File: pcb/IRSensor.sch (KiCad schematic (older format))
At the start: 39 parts, among them Q2 IRFML8244, Q3 IRFML8244, U2 NJM2746, U3 NJU7098, U4 NJU7098, U5 NJU7098, U6 NJU7098

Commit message: Make netlist
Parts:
- C10, C11, C4, C5, C6, C7, C8, C9: footprint (none) -> Capacitors_SMD:C_0603_HandSoldering
- D2, D3, D4, D5, D6, D7, D8, D9: footprint (none) -> LEDs:LED_D5.0mm_Horizontal_O1.27mm_Z3.0mm
- Q2, Q3: footprint (none) -> TO_SOT_Packages_SMD:SOT-23
- R10, R11, R12, R13, R16, R17, R18, R19, R20, R21, R22, R23, R8, R9: footprint (none) -> Resistors_SMD:R_0603_HandSoldering
- R14, R15: footprint (none) -> Resistors_SMD:R_0805_HandSoldering
- U3, U4, U5, U6: footprint Package_TO_SOT_SMD:TSOT-23-6 -> TO_SOT_Packages_SMD:SOT-23-6_Handsoldering
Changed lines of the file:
@@
 F 0 "R8" H 1320 1796 50  0000 L CNN
 F 1 "10k" V 1250 1700 50  0000 L CNN
-F 2 "" V 1180 1750 50  0001 C CNN
+F 2 "Resistors_SMD:R_0603_HandSoldering" V 1180 1750 50  0001 C CNN
 F 3 "~" H 1250 1750 50  0001 C CNN
 	1    1250 1750
@@
 F 0 "R9" H 1320 2096 50  0000 L CNN
 F 1 "10k" V 1250 2000 50  0000 L CNN
-F 2 "" V 1180 2050 50  0001 C CNN
+F 2 "Resistors_SMD:R_0603_HandSoldering" V 1180 2050 50  0001 C CNN
 F 3 "~" H 1250 2050 50  0001 C CNN
 	1    1250 2050
@@
 F 0 "R10" H 1320 3596 50  0000 L CNN
 F 1 "10k" V 1250 3500 50  0000 L CNN
-F 2 "" V 1180 3550 50  0001 C CNN
+F 2 "Resistors_SMD:R_0603_HandSoldering" V 1180 3550 50  0001 C CNN
 F 3 "~" H 1250 3550 50  0001 C CNN
 	1    1250 3550
@@
 F 0 "R11" H 1320 3896 50  0000 L CNN
 F 1 "10k" V 1250 3800 50  0000 L CNN
-F 2 "" V 1180 3850 50  0001 C CNN
+F 2 "Resistors_SMD:R_0603_HandSoldering" V 1180 3850 50  0001 C CNN
 F 3 "~" H 1250 3850 50  0001 C CNN
 	1    1250 3850
@@
 F 0 "R12" V 2550 1950 50  0000 L CNN
 F 1 "10" V 2650 1950 50  0000 L CNN
-F 2 "" V 2580 2000 50  0001 C CNN
+F 2 "Resistors_SMD:R_0603_HandSoldering" V 2580 2000 50  0001 C CNN
 F 3 "~" H 2650 2000 50  0001 C CNN
 	1    2650 2000
@@
 F 0 "R13" V 2550 3750 50  0000 L CNN
 F 1 "10" V 2650 3750 50  0000 L CNN
-F 2 "" V 2580 3800 50  0001 C CNN
+F 2 "Resistors_SMD:R_0603_HandSoldering" V 2580 3800 50  0001 C CNN
 F 3 "~" H 2650 3800 50  0001 C CNN
 	1    2650 3800
@@
 F 0 "D2" V 3139 1232 50  0000 R CNN
 F 1 "VSLY5850" V 3048 1232 50  0000 R CNN
-F 2 "" H 3100 1350 50  0001 C CNN
+F 2 "LEDs:LED_D5.0mm_Horizontal_O1.27mm_Z3.0mm" H 3100 1350 50  0001 C CNN
 F 3 "~" H 3100 1350 50  0001 C CNN
 	1    3100 1350
@@
 F 0 "D3" V 3139 1532 50  0000 R CNN
 F 1 "VSLY5850" V 3048 1532 50  0000 R CNN
-F 2 "" H 3100 1650 50  0001 C CNN
+F 2 "LEDs:LED_D5.0mm_Horizontal_O1.27mm_Z3.0mm" H 3100 1650 50  0001 C CNN
 F 3 "~" H 3100 1650 50  0001 C CNN
 	1    3100 1650
@@
 F 0 "D4" V 3139 3032 50  0000 R CNN
 F 1 "VSLY5850" V 3048 3032 50  0000 R CNN
-F 2 "" H 3100 3150 50  0001 C CNN
+F 2 "LEDs:LED_D5.0mm_Horizontal_O1.27mm_Z3.0mm" H 3100 3150 50  0001 C CNN
 F 3 "~" H 3100 3150 50  0001 C CNN
 	1    3100 3150
@@
 F 0 "D5" V 3139 3332 50  0000 R CNN
 F 1 "VSLY5850" V 3048 3332 50  0000 R CNN
-F 2 "" H 3100 3450 50  0001 C CNN
+F 2 "LEDs:LED_D5.0mm_Horizontal_O1.27mm_Z3.0mm" H 3100 3450 50  0001 C CNN
 F 3 "~" H 3100 3450 50  0001 C CNN
 	1    3100 3450
@@
 F 0 "Q3" H 3204 3846 50  0000 L CNN
 F 1 "IRFML8244" H 3204 3755 50  0000 L CNN
-F 2 "" H 3200 3900 50  0001 C CNN
+F 2 "TO_SOT_Packages_SMD:SOT-23" H 3200 3900 50  0001 C CNN
 F 3 "~" H 3000 3800 50  0001 C CNN
 	1    3000 3800
@@
 F 0 "R15" H 2900 4050 50  0000 L CNN
 F 1 "15 1/4W" H 2650 4150 50  0000 L CNN
-F 2 "" V 3030 4150 50  0001 C CNN
+F 2 "Resistors_SMD:R_0805_HandSoldering" V 3030 4150 50  0001 C CNN
 F 3 "~" H 3100 4150 50  0001 C CNN
 	1    3100 4150
@@
 F 0 "Q2" H 3204 2046 50  0000 L CNN
 F 1 "IRFML8244" H 3204 1955 50  0000 L CNN
-F 2 "" H 3200 2100 50  0001 C CNN
+F 2 "TO_SOT_Packages_SMD:SOT-23" H 3200 2100 50  0001 C CNN
 F 3 "~" H 3000 2000 50  0001 C CNN
 	1    3000 2000
@@
 F 0 "R14" H 2900 2250 50  0000 L CNN
 F 1 "15 1/4W" H 2650 2350 50  0000 L CNN
-F 2 "" V 3030 2350 50  0001 C CNN
+F 2 "Resistors_SMD:R_0805_HandSoldering" V 3030 2350 50  0001 C CNN
 F 3 "~" H 3100 2350 50  0001 C CNN
 	1    3100 2350
@@
 F 0 "D6" V 5596 1520 50  0000 R CNN
 F 1 "SFH213FA" V 5505 1520 50  0000 R CNN
-F 2 "" H 5550 1600 50  0001 C CNN
+F 2 "LEDs:LED_D5.0mm_Horizontal_O1.27mm_Z3.0mm" H 5550 1600 50  0001 C CNN
 F 3 "~" H 5550 1600 50  0001 C CNN
 	1    5550 1600
@@
 F 0 "C4" V 6000 1950 50  0000 C CNN
 F 1 "0.01u" V 5700 1950 50  0000 C CNN
-F 2 "" H 5888 1800 50  0001 C CNN
+F 2 "Capacitors_SMD:C_0603_HandSoldering" H 5888 1800 50  0001 C CNN
 F 3 "~" H 5850 1950 50  0001 C CNN
 	1    5850 1950
@@
 F 0 "R17" V 6450 1200 50  0000 C CNN
 F 1 "220k" V 6550 1200 50  0000 C CNN
-F 2 "" V 6480 1200 50  0001 C CNN
+F 2 "Resistors_SMD:R_0603_HandSoldering" V 6480 1200 50  0001 C CNN
 F 3 "~" H 6550 1200 50  0001 C CNN
 	1    6550 1200
@@
 F 0 "C5" V 6700 850 50  0000 C CNN
 F 1 "22p" V 6400 850 50  0000 C CNN
-F 2 "" H 6588 700 50  0001 C CNN
+F 2 "Capacitors_SMD:C_0603_HandSoldering" H 6588 700 50  0001 C CNN
 F 3 "~" H 6550 850 50  0001 C CNN
 	1    6550 850
@@
 F 0 "R16" V 5450 2100 50  0000 C CNN
 F 1 "100k" V 5550 2100 50  0000 C CNN
-F 2 "" V 5480 2100 50  0001 C CNN
+F 2 "Resistors_SMD:R_0603_HandSoldering" V 5480 2100 50  0001 C CNN
 F 3 "~" H 5550 2100 50  0001 C CNN
 	1    5550 2100
@@
 F 0 "U3" H 6994 1896 50  0000 L CNN
 F 1 "NJU7098" H 6994 1805 50  0000 L CNN
-F 2 "Package_TO_SOT_SMD:TSOT-23-6" H 6650 1250 50  0001 C CNN
+F 2 "TO_SOT_Packages_SMD:SOT-23-6_Handsoldering" H 6650 1250 50  0001 C CNN
 F 3 "https://www.analog.com/media/en/technical-documentation/data-sheets/LTC6228-6229.pdf" H 6650 1850 50  0001 C CNN
 	1    6650 1850
@@
 F 0 "D7" V 5596 3420 50  0000 R CNN
 F 1 "SFH213FA" V 5505 3420 50  0000 R CNN
-F 2 "" H 5550 3500 50  0001 C CNN
+F 2 "LEDs:LED_D5.0mm_Horizontal_O1.27mm_Z3.0mm" H 5550 3500 50  0001 C CNN
 F 3 "~" H 5550 3500 50  0001 C CNN
 	1    5550 3500
@@
 F 0 "C6" V 6000 3850 50  0000 C CNN
 F 1 "0.01u" V 5700 3850 50  0000 C CNN
-F 2 "" H 5888 3700 50  0001 C CNN
+F 2 "Capacitors_SMD:C_0603_HandSoldering" H 5888 3700 50  0001 C CNN
 F 3 "~" H 5850 3850 50  0001 C CNN
 	1    5850 3850
@@
 F 0 "R19" V 6450 3100 50  0000 C CNN
 F 1 "220k" V 6550 3100 50  0000 C CNN
-F 2 "" V 6480 3100 50  0001 C CNN
+F 2 "Resistors_SMD:R_0603_HandSoldering" V 6480 3100 50  0001 C CNN
 F 3 "~" H 6550 3100 50  0001 C CNN
 	1    6550 3100
@@
 F 0 "C7" V 6700 2750 50  0000 C CNN
 F 1 "22p" V 6400 2750 50  0000 C CNN
-F 2 "" H 6588 2600 50  0001 C CNN
+F 2 "Capacitors_SMD:C_0603_HandSoldering" H 6588 2600 50  0001 C CNN
 F 3 "~" H 6550 2750 50  0001 C CNN
 	1    6550 2750
@@
 F 0 "R18" V 5450 4000 50  0000 C CNN
 F 1 "100k" V 5550 4000 50  0000 C CNN
-F 2 "" V 5480 4000 50  0001 C CNN
+F 2 "Resistors_SMD:R_0603_HandSoldering" V 5480 4000 50  0001 C CNN
 F 3 "~" H 5550 4000 50  0001 C CNN
 	1    5550 4000
@@
 F 0 "U4" H 6994 3796 50  0000 L CNN
 F 1 "NJU7098" H 6994 3705 50  0000 L CNN
-F 2 "Package_TO_SOT_SMD:TSOT-23-6" H 6650 3150 50  0001 C CNN
+F 2 "TO_SOT_Packages_SMD:SOT-23-6_Handsoldering" H 6650 3150 50  0001 C CNN
 F 3 "https://www.analog.com/media/en/technical-documentation/data-sheets/LTC6228-6229.pdf" H 6650 3750 50  0001 C CNN
 	1    6650 3750
@@
 F 0 "D8" V 8246 1520 50  0000 R CNN
 F 1 "SFH213FA" V 8155 1520 50  0000 R CNN
-F 2 "" H 8200 1600 50  0001 C CNN
+F 2 "LEDs:LED_D5.0mm_Horizontal_O1.27mm_Z3.0mm" H 8200 1600 50  0001 C CNN
 F 3 "~" H 8200 1600 50  0001 C CNN
 	1    8200 1600
@@
 F 0 "C8" V 8650 1950 50  0000 C CNN
 F 1 "0.01u" V 8350 1950 50  0000 C CNN
-F 2 "" H 8538 1800 50  0001 C CNN
+F 2 "Capacitors_SMD:C_0603_HandSoldering" H 8538 1800 50  0001 C CNN
 F 3 "~" H 8500 1950 50  0001 C CNN
 	1    8500 1950
@@
 F 0 "R22" V 9100 1200 50  0000 C CNN
 F 1 "220k" V 9200 1200 50  0000 C CNN
-F 2 "" V 9130 1200 50  0001 C CNN
+F 2 "Resistors_SMD:R_0603_HandSoldering" V 9130 1200 50  0001 C CNN
 F 3 "~" H 9200 1200 50  0001 C CNN
 	1    9200 1200
@@
 F 0 "C10" V 9350 850 50  0000 C CNN
 F 1 "22p" V 9050 850 50  0000 C CNN
-F 2 "" H 9238 700 50  0001 C CNN
+F 2 "Capacitors_SMD:C_0603_HandSoldering" H 9238 700 50  0001 C CNN
 F 3 "~" H 9200 850 50  0001 C CNN
 	1    9200 850
@@
 F 0 "R20" V 8100 2100 50  0000 C CNN
 F 1 "100k" V 8200 2100 50  0000 C CNN
-F 2 "" V 8130 2100 50  0001 C CNN
+F 2 "Resistors_SMD:R_0603_HandSoldering" V 8130 2100 50  0001 C CNN
 F 3 "~" H 8200 2100 50  0001 C CNN
 	1    8200 2100
@@
 F 0 "U5" H 9644 1896 50  0000 L CNN
 F 1 "NJU7098" H 9644 1805 50  0000 L CNN
-F 2 "Package_TO_SOT_SMD:TSOT-23-6" H 9300 1250 50  0001 C CNN
+F 2 "TO_SOT_Packages_SMD:SOT-23-6_Handsoldering" H 9300 1250 50  0001 C CNN
 F 3 "https://www.analog.com/media/en/technical-documentation/data-sheets/LTC6228-6229.pdf" H 9300 1850 50  0001 C CNN
 	1    9300 1850
@@
 F 0 "D9" V 8246 3420 50  0000 R CNN
 F 1 "SFH213FA" V 8155 3420 50  0000 R CNN
-F 2 "" H 8200 3500 50  0001 C CNN
+F 2 "LEDs:LED_D5.0mm_Horizontal_O1.27mm_Z3.0mm" H 8200 3500 50  0001 C CNN
 F 3 "~" H 8200 3500 50  0001 C CNN
 	1    8200 3500
@@
 F 0 "C9" V 8650 3850 50  0000 C CNN
 F 1 "0.01u" V 8350 3850 50  0000 C CNN
-F 2 "" H 8538 3700 50  0001 C CNN
+F 2 "Capacitors_SMD:C_0603_HandSoldering" H 8538 3700 50  0001 C CNN
 F 3 "~" H 8500 3850 50  0001 C CNN
 	1    8500 3850
@@
 F 0 "R23" V 9100 3100 50  0000 C CNN
 F 1 "220k" V 9200 3100 50  0000 C CNN
-F 2 "" V 9130 3100 50  0001 C CNN
+F 2 "Resistors_SMD:R_0603_HandSoldering" V 9130 3100 50  0001 C CNN
 F 3 "~" H 9200 3100 50  0001 C CNN
 	1    9200 3100
@@
 F 0 "C11" V 9350 2750 50  0000 C CNN
 F 1 "22p" V 9050 2750 50  0000 C CNN
-F 2 "" H 9238 2600 50  0001 C CNN
+F 2 "Capacitors_SMD:C_0603_HandSoldering" H 9238 2600 50  0001 C CNN
 F 3 "~" H 9200 2750 50  0001 C CNN
 	1    9200 2750
@@
 F 0 "R21" V 8100 4000 50  0000 C CNN
 F 1 "100k" V 8200 4000 50  0000 C CNN
-F 2 "" V 8130 4000 50  0001 C CNN
+F 2 "Resistors_SMD:R_0603_HandSoldering" V 8130 4000 50  0001 C CNN
 F 3 "~" H 8200 4000 50  0001 C CNN
 	1    8200 4000
@@
 F 0 "U6" H 9644 3796 50  0000 L CNN
 F 1 "NJU7098" H 9644 3705 50  0000 L CNN
-F 2 "Package_TO_SOT_SMD:TSOT-23-6" H 9300 3150 50  0001 C CNN
+F 2 "TO_SOT_Packages_SMD:SOT-23-6_Handsoldering" H 9300 3150 50  0001 C CNN
 F 3 "https://www.analog.com/media/en/technical-documentation/data-sheets/LTC6228-6229.pdf" H 9300 3750 50  0001 C CNN
 	1    9300 3750

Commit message: Update pcb
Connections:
- net +3.3VA: now also D6.1 (K), D7.1 (K), D8.1 (K), D9.1 (K); no longer D6.2 (A), D7.2 (A), D8.2 (A), D9.2 (A)
- net at C4.2, R16.2: now also D6.2 (A); no longer D6.1 (K)
- net at C6.2, R18.2: now also D7.2 (A); no longer D7.1 (K)
- net at C8.2, R20.2: now also D8.2 (A); no longer D8.1 (K)
- net at C9.2, R21.2: now also D9.2 (A); no longer D9.1 (K)
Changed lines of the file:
@@
 F 3 "~" H 5550 1600 50  0001 C CNN
 	1    5550 1600
-	0    -1   -1   0
+	0    1    1    0
 $EndComp
 $Comp
@@
 F 3 "~" H 5550 3500 50  0001 C CNN
 	1    5550 3500
-	0    -1   -1   0
+	0    1    1    0
 $EndComp
 $Comp
@@
 F 3 "~" H 8200 1600 50  0001 C CNN
 	1    8200 1600
-	0    -1   -1   0
+	0    1    1    0
 $EndComp
 $Comp
@@
 F 3 "~" H 8200 3500 50  0001 C CNN
 	1    8200 3500
-	0    -1   -1   0
-$EndComp
-$Comp
+	0    1    1    0
+$EndComp
+$Comp

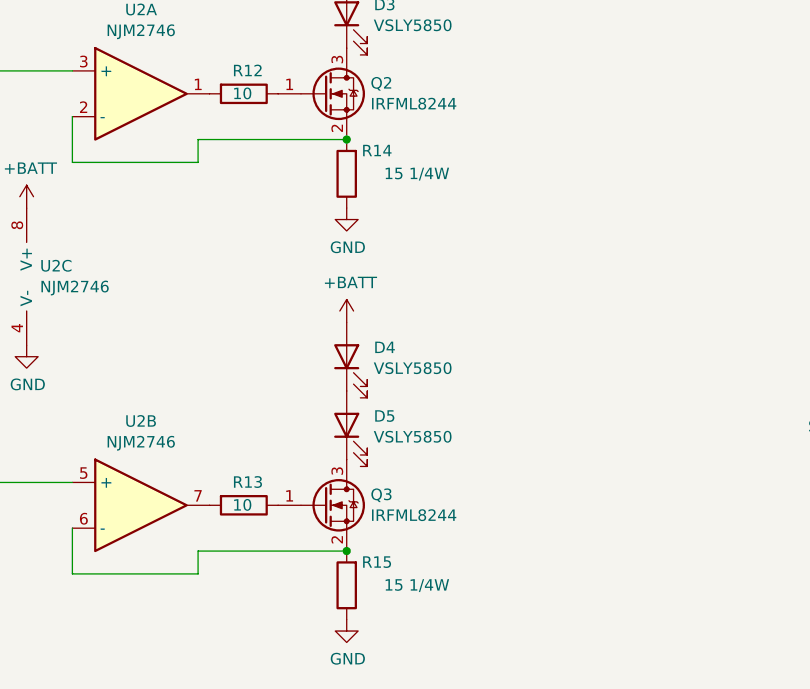
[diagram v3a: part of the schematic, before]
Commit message: Write about where to buy the parts
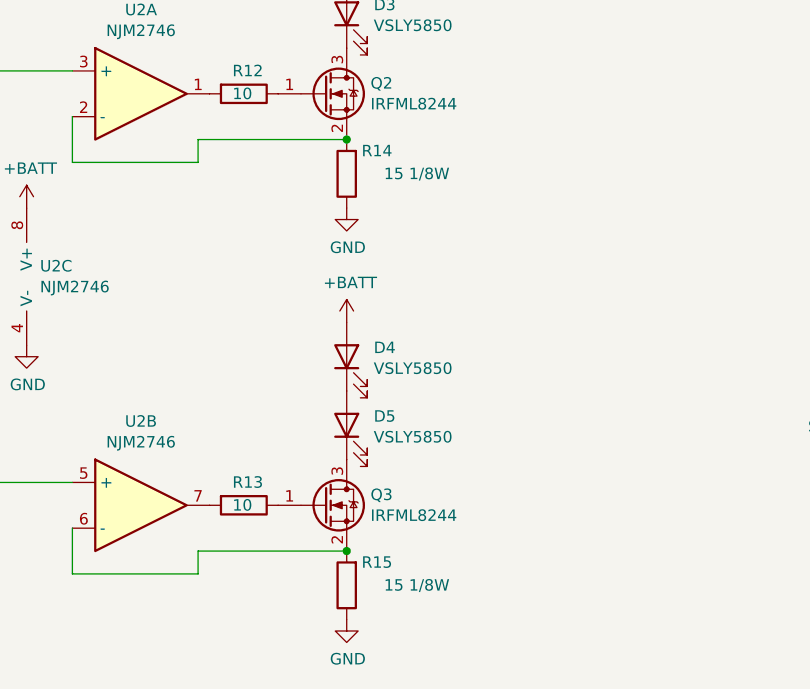
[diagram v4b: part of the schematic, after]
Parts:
- C10, C11, C5, C7: Buy (none) -> https://akizukidenshi.com/catalog/g/gP-13313/; Vendor (none) -> https://akizukidenshi.com/catalog/g/gP-13313/
- C4, C6, C8, C9: Buy (none) -> https://akizukidenshi.com/catalog/g/gP-13387/; Vendor (none) -> https://akizukidenshi.com/catalog/g/gP-13387/
- D2, D3, D4, D5: Buy (none) -> https://www.digikey.jp/ja/products/detail/vishay-semiconduc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; Vendor (none) -> https://www.digikey.jp/ja/products/detail/vishay-semiconduc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
- D6, D7, D8, D9: Buy (none) -> https://www.digikey.jp/ja/products/detail/osram-opto-semico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; Vendor (none) -> https://www.digikey.jp/ja/products/detail/osram-opto-semico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
- Q2, Q3: Buy (none) -> https://akizukidenshi.com/catalog/g/gI-06051/; Vendor (none) -> https://akizukidenshi.com/catalog/g/gI-06051/
- R14, R15: value 15 1/4W -> 15 1/8W; Buy (none) -> https://www.sengoku.co.jp/mod/sgk_cart/detail.php?code=EEHD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; Vendor (none) -> https://www.sengoku.co.jp/mod/sgk_cart/detail.php?code=EEHD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
- U2: Buy (none) -> https://akizukidenshi.com/catalog/g/gI-09495/; Vendor (none) -> https://akizukidenshi.com/catalog/g/gI-09495/
- U3, U4, U5, U6: Buy (none) -> https://akizukidenshi.com/catalog/g/gI-14988/; Vendor (none) -> https://akizukidenshi.com/catalog/g/gI-14988/
